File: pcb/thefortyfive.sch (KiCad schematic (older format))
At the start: 117 parts, among them J1 Conn_01x16_Female, J2 Conn_01x12_Female

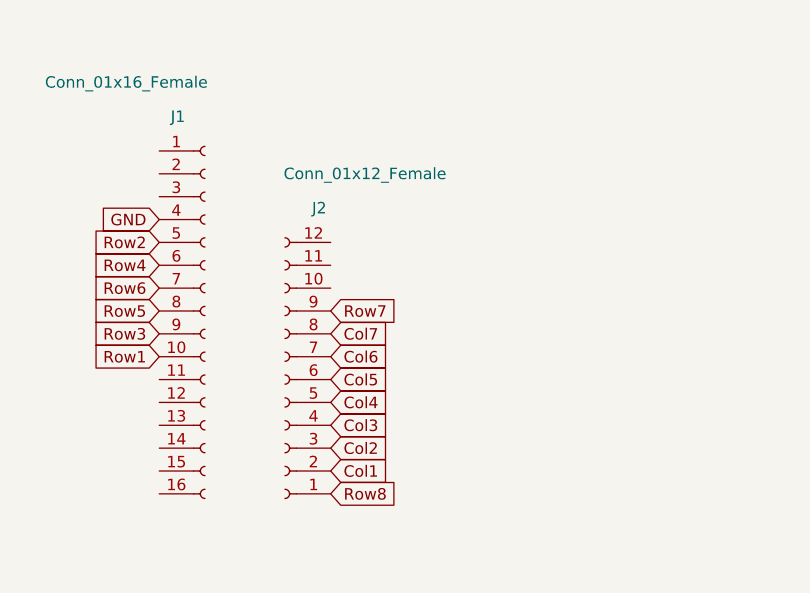
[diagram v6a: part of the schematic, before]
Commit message: fix issue with reversed connector
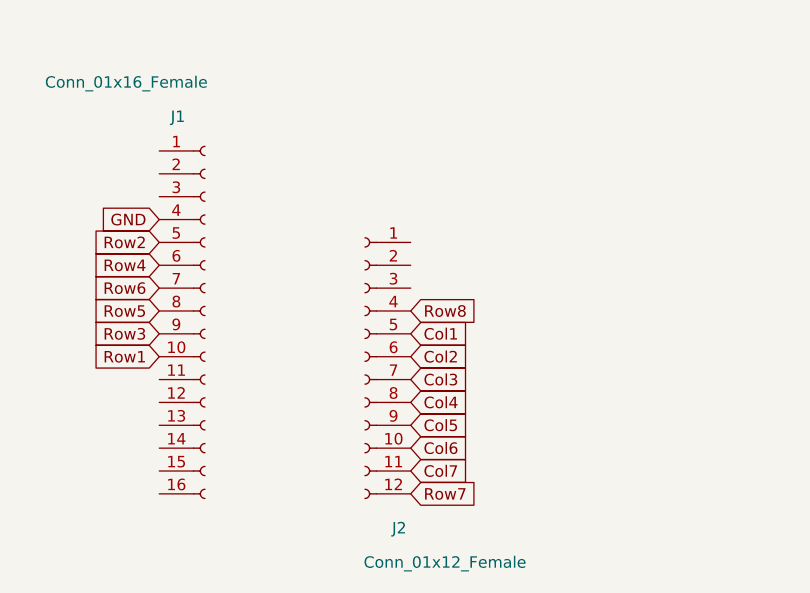
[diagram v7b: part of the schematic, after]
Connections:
- net Col1: now also J2.5 (Pin_5); no longer J2.2 (Pin_2)
- net Col2: now also J2.6 (Pin_6); no longer J2.3 (Pin_3)
- net Col3: now also J2.7 (Pin_7); no longer J2.4 (Pin_4)
- net Col4: now also J2.8 (Pin_8); no longer J2.5 (Pin_5)
- net Col5: now also J2.9 (Pin_9); no longer J2.6 (Pin_6)
- net Col6: now also J2.10 (Pin_10); no longer J2.7 (Pin_7)
- net Col7: now also J2.11 (Pin_11); no longer J2.8 (Pin_8)
- net Row7: now also J2.12 (Pin_12); no longer J2.9 (Pin_9)
- net Row8: now also J2.4 (Pin_4); no longer J2.1 (Pin_1)
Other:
- moved on the sheet: J2
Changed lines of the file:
@@
 L Connector:Conn_01x12_Female J2
 U 1 1 5E6E03D7
-P 6150 9150
-F 0 "J2" H 6000 8400 50  0000 C CNN
-F 1 "Conn_01x12_Female" H 5800 8250 50  0000 C CNN
-F 2 "Connector_PinSocket_2.54mm:PinSocket_1x12_P2.54mm_Vertical" H 6150 9150 50  0001 C CNN
-F 3 "~" H 6150 9150 50  0001 C CNN
-	1    6150 9150
-	-1   0    0    1
+P 6500 9050
+F 0 "J2" H 6350 8300 50  0000 C CNN
+F 1 "Conn_01x12_Female" H 6150 8150 50  0000 C CNN
+F 2 "Connector_PinSocket_2.54mm:PinSocket_1x12_P2.54mm_Vertical" H 6500 9050 50  0001 C CNN
+F 3 "~" H 6500 9050 50  0001 C CNN
+	1    6500 9050
+	-1   0    0    -1
 $EndComp
 $Comp
@@
 Text GLabel 5600 8750 0    50   Input ~ 0
 Row6
-Text GLabel 6350 8850 2    50   Input ~ 0
-Row7
-Text GLabel 6350 9650 2    50   Input ~ 0
+Text GLabel 6700 8850 2    50   Input ~ 0
 Row8
-Text GLabel 6350 9550 2    50   Input ~ 0
+Text GLabel 6700 8950 2    50   Input ~ 0
 Col1
-Text GLabel 6350 9450 2    50   Input ~ 0
+Text GLabel 6700 9050 2    50   Input ~ 0
 Col2
-Text GLabel 6350 9350 2    50   Input ~ 0
+Text GLabel 6700 9150 2    50   Input ~ 0
 Col3
-Text GLabel 6350 9250 2    50   Input ~ 0
+Text GLabel 6700 9250 2    50   Input ~ 0
 Col4
-Text GLabel 6350 9150 2    50   Input ~ 0
+Text GLabel 6700 9350 2    50   Input ~ 0
 Col5
-Text GLabel 6350 9050 2    50   Input ~ 0
+Text GLabel 6700 9450 2    50   Input ~ 0
 Col6
-Text GLabel 6350 8950 2    50   Input ~ 0
+Text GLabel 6700 9550 2    50   Input ~ 0
 Col7
 $Comp
@@
 Text GLabel 5600 8450 0    50   Input ~ 0
 GND
+Text GLabel 6700 9650 2    50   Input ~ 0
+Row7
 $EndSCHEMATC

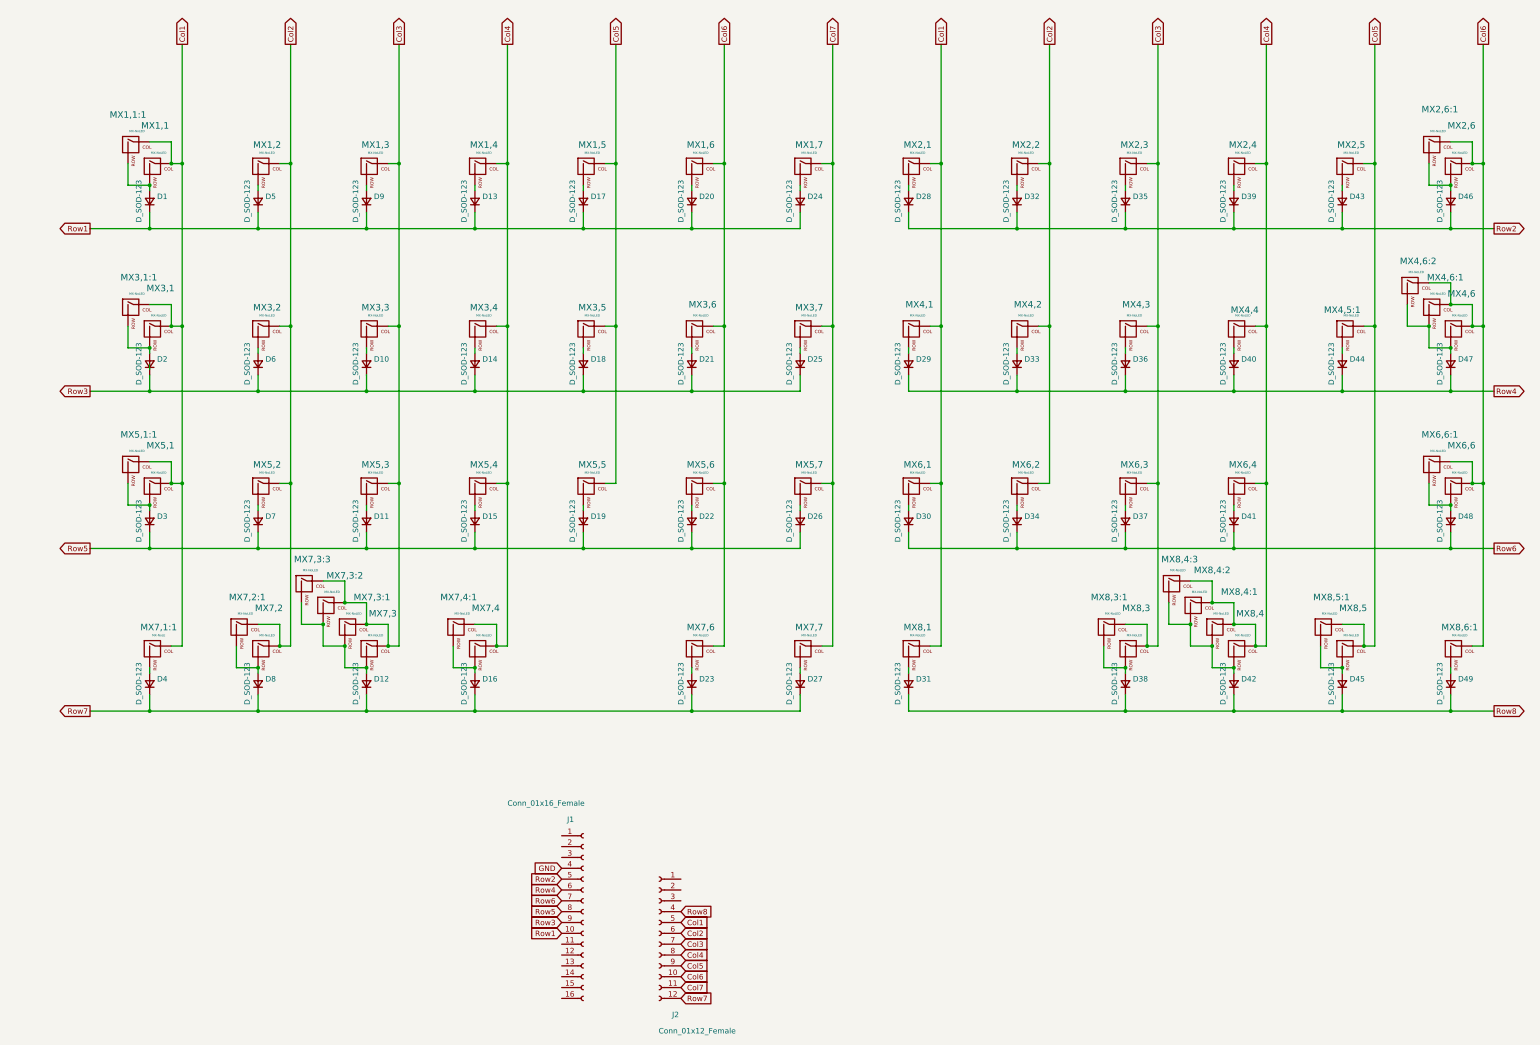
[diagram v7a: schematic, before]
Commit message: remove all switch options
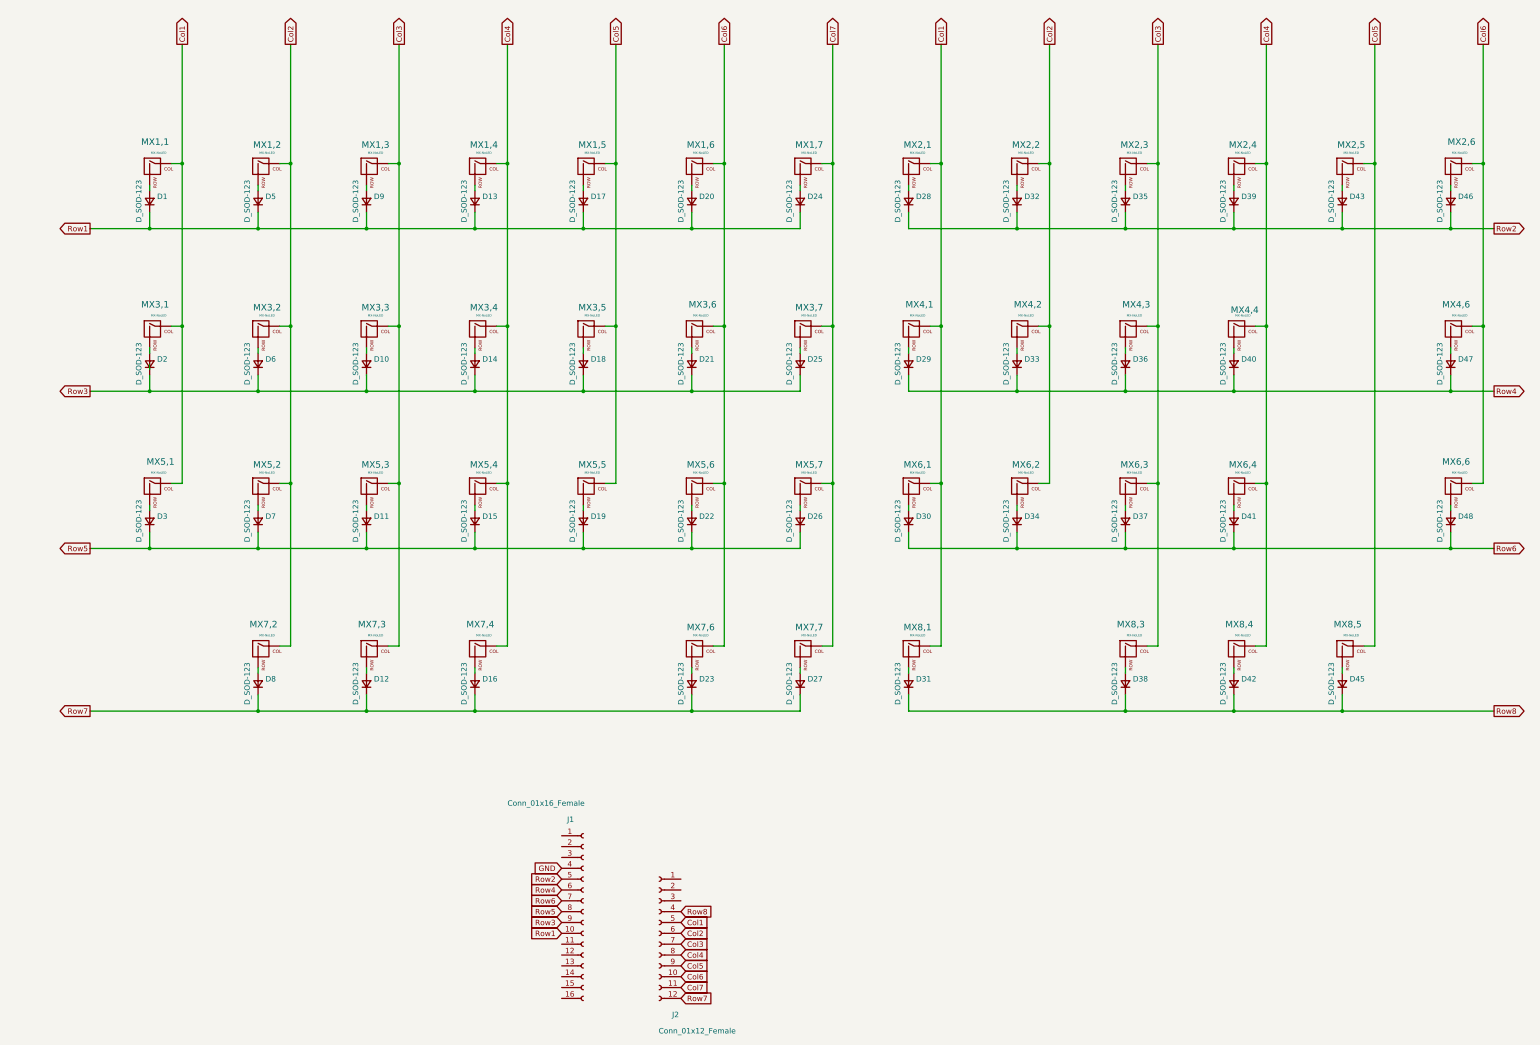
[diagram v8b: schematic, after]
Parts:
- removed D4, D44, D49: D_SOD-123, Diode_SMD:D_SOD-123, symbol Device:D_Small
- removed MX1,1:1, MX2,6:1: MX-NoLED, MX_Alps_Hybrid:MXOnly-1.5U-NoLED, symbol MX_Alps_Hybrid:MX-NoLED
- removed MX3,1:1, MX6,6:1: MX-NoLED, MX_Alps_Hybrid:MXOnly-1.75U-NoLED, symbol MX_Alps_Hybrid:MX-NoLED
- removed MX4,5:1, MX7,2:1, MX7,3:1, MX7,3:2, MX8,4:1, MX8,4:2, MX8,5:1: MX-NoLED, MX_Alps_Hybrid:MXOnly-1U-NoLED, symbol MX_Alps_Hybrid:MX-NoLED
- removed MX4,6:1, MX5,1:1: MX-NoLED, MX_Alps_Hybrid:MXOnly-2.25U-NoLED, symbol MX_Alps_Hybrid:MX-NoLED
- removed MX4,6:2, MX7,3:3, MX7,4:1, MX8,3:1, MX8,4:3, MX8,6:1: MX-NoLED, MX_Alps_Hybrid:MXOnly-1.25U-NoLED, symbol MX_Alps_Hybrid:MX-NoLED
- removed MX7,1:1: MX-NoLE, MX_Alps_Hybrid:MXOnly-1.25U-NoLED, symbol MX_Alps_Hybrid:MX-NoLED
